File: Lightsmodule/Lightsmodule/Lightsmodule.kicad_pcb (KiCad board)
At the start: 2 copper layers, 69 x 45.5 mm, 33 parts, among them J1 Conn_01x02_Socket, J2 Conn_01x06_Socket, Q5 Q_NMOS_GSD, SW1 SW_Push_SPDT, SW2 SW_Push_SPDT, SW3 SW_Push_SPDT, SW6 SW_Push_SPDT, SW7 SW_Push_SPDT, SW8 SW_Push_SPDT, U1 TLC555xD, U2 TLP3553A, U3 TLP3553A

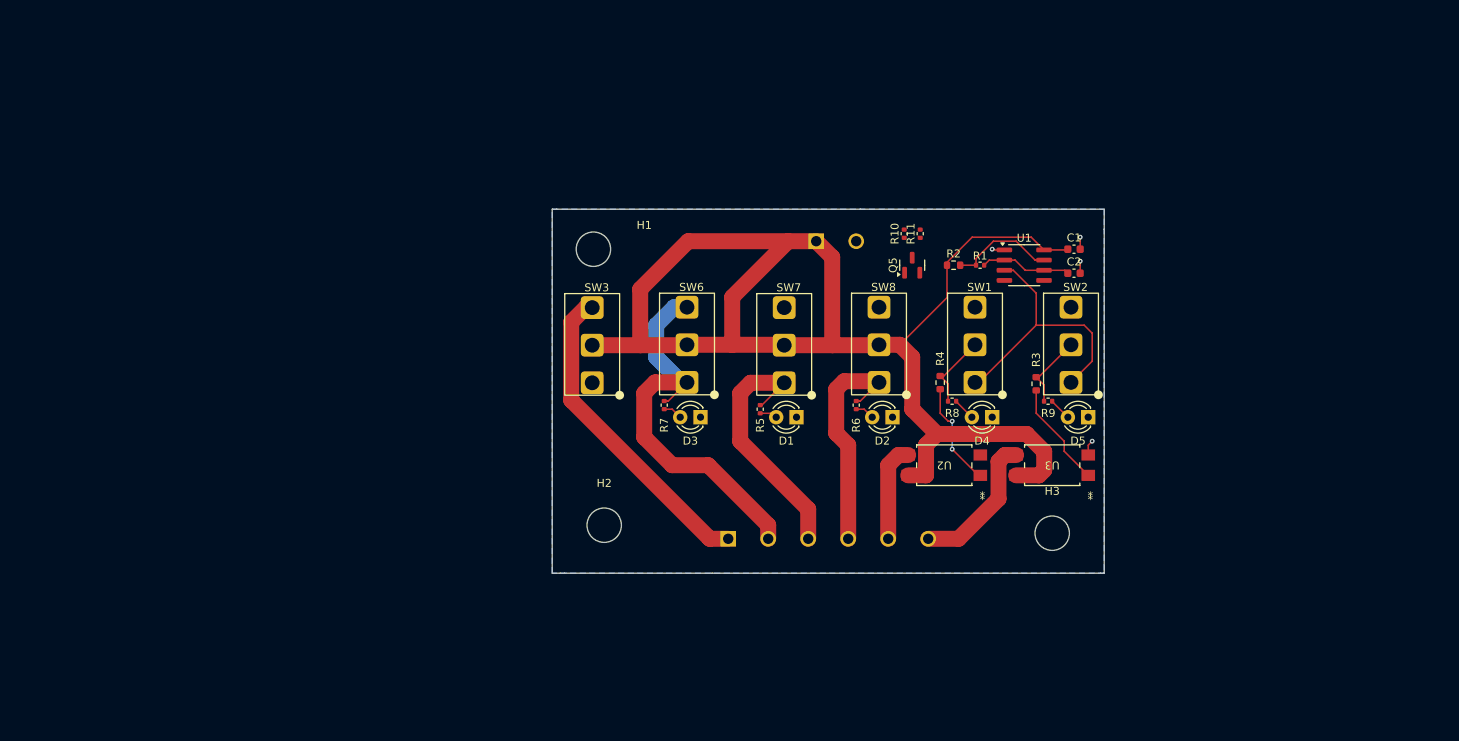
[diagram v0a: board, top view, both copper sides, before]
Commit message: In Theory working Timing / Buzzer Circuit
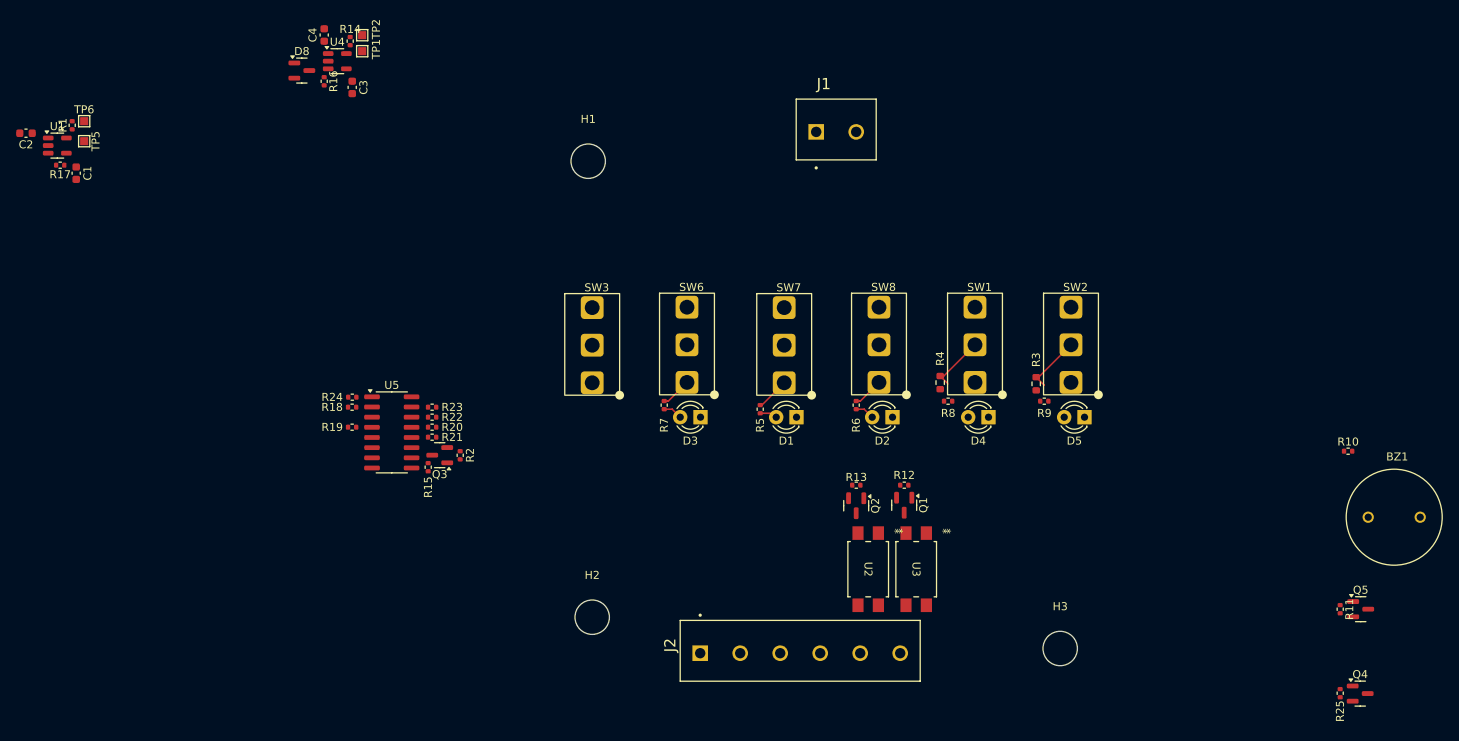
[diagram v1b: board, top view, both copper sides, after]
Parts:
- added BZ1: Buzzer, Library:CUI_CEM-1212S, F.Cu at (280.2, 116.5)
- added C3: 820n, Capacitor_SMD:C_0603_1608Metric, F.Cu at (150.0, 62.8)
- added C4: 820n, Capacitor_SMD:C_0603_1608Metric, F.Cu at (146.5, 56.2)
- added D8: D_Zener_Dual_CommonCathode_AAK, Package_TO_SOT_SMD:SOT-23, F.Cu at (143.7, 60.7)
- added Q1: Q_NMOS_GSD, Package_TO_SOT_SMD:SOT-23, F.Cu at (219.0, 115.0)
- added Q2: Q_NMOS_GSD, Package_TO_SOT_SMD:SOT-23, F.Cu at (213.0, 115.1)
- added Q3: Q_NMOS_GSD, Package_TO_SOT_SMD:SOT-23, F.Cu at (160.9, 108.8)
- added Q4: Q_NMOS_GSD, Package_TO_SOT_SMD:SOT-23, F.Cu at (276.0, 138.6)
- added R12: 325k, Resistor_SMD:R_0402_1005Metric, F.Cu at (219.0, 112.5)
- added R13: 325k, Resistor_SMD:R_0402_1005Metric, F.Cu at (213.0, 112.5)
- added R14: 325k, Resistor_SMD:R_0402_1005Metric, F.Cu at (149.8, 57.0)
- added R15: 325k, Resistor_SMD:R_0402_1005Metric, F.Cu at (159.5, 110.2)
- added R16: 820k, Resistor_SMD:R_0402_1005Metric, F.Cu at (146.5, 62.0)
- added R17: 820k, Resistor_SMD:R_0402_1005Metric, F.Cu at (113.5, 72.5)
- added R18: 0, Resistor_SMD:R_0402_1005Metric, F.Cu at (150.0, 102.8)
- added R19: 0, Resistor_SMD:R_0402_1005Metric, F.Cu at (150.0, 105.2)
- added R20: 0, Resistor_SMD:R_0402_1005Metric, F.Cu at (160.0, 105.2)
- added R21: 0, Resistor_SMD:R_0402_1005Metric, F.Cu at (160.0, 106.5)
- added R22: 0, Resistor_SMD:R_0402_1005Metric, F.Cu at (160.0, 104.0)
- added R23: 0, Resistor_SMD:R_0402_1005Metric, F.Cu at (160.0, 102.8)
- added R24: 0, Resistor_SMD:R_0402_1005Metric, F.Cu at (150.0, 101.5)
- added R25: 325k, Resistor_SMD:R_0402_1005Metric, F.Cu at (273.5, 138.5)
- added TP1: TestPoint, TestPoint:TestPoint_Pad_1.0x1.0mm, F.Cu at (151.2, 58.2)
- added TP2: TestPoint, TestPoint:TestPoint_Pad_1.0x1.0mm, F.Cu at (151.2, 56.2)
- added TP5: TestPoint, TestPoint:TestPoint_Pad_1.0x1.0mm, F.Cu at (116.5, 69.5)
- added TP6: TestPoint, TestPoint:TestPoint_Pad_1.0x1.0mm, F.Cu at (116.5, 67.0)
- added U4: MIC1553, Package_TO_SOT_SMD:SOT-23-5, F.Cu at (148.1, 59.5)
- added U5: MC14040BDR2G, Package_SO:SOIC-16_3.9x9.9mm_P1.27mm, F.Cu at (154.9, 105.9)
- C1, C2: value 470n -> 820n
- J1, J2: moved to F.Cu
- R1, R10: value 2M -> 820k
- R11: value 2M -> 325k
- R2: value 1.8k -> 325k; footprint Resistor_SMD:R_0603_1608Metric -> Resistor_SMD:R_0402_1005Metric
- U1: value TLC555xD -> MIC1553; footprint Package_SO:SOIC-8_3.9x4.9mm_P1.27mm -> Package_TO_SOT_SMD:SOT-23-5
- moved C2 132.2 mm to (109.2, 68.5), turned to 180 degrees
- moved C1 125.1 mm to (115.5, 73.5), turned to -90 degrees
- moved U1 121.8 mm to (113.1, 70.0)
- moved R1 114.8 mm to (115.0, 67.5), turned to 90 degrees
- moved Q5 70.7 mm to (276.1, 128.0), turned to 0 degrees
- moved R11 70.4 mm to (273.5, 128.0), turned to -90 degrees
- moved R2 66.1 mm to (163.5, 108.8), turned to 90 degrees
- moved R10 61.8 mm to (274.5, 108.2), turned to 0 degrees
- moved U3 21.4 mm to (220.5, 123.0), turned to -90 degrees
- moved U2 16.1 mm to (214.5, 123.0), turned to -90 degrees
- moved J2 14.7 mm to (193.5, 133.5)
- moved H3 14.4 mm to (238.5, 132.9)
- moved J1 13.7 mm to (208.0, 68.3)
- moved H2 11.6 mm to (180.0, 129.0)
- moved H1 11.0 mm to (179.5, 72.0)
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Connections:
- C2 pad 1: Net-(U1-THR) -> Net-(U1-T/T)
- Q5 pad 1: /OUT -> /BUZZ_DRV
- Q5 pad 2: GND -> Net-(Q4-D)
- R1 pad 1: Net-(U1-DIS) -> /1hz
- R1 pad 2: Net-(U1-THR) -> Net-(U1-T/T)
- R11 pad 1: /OUT -> /BUZZ_DRV
- R2 pad 1: +12V -> /1hz
- R2 pad 2: Net-(U1-DIS) -> GND
- R3 pad 1: /RIGHT_EN -> +12V
- R4 pad 1: /LEFT_EN -> +12V
- SW1 pad 1: /OUT -> /1hz
- SW2 pad 1: /OUT -> /1hz
- U1 pad 1: GND -> Net-(U1-T/T)
- U1 pad 2: Net-(U1-THR) -> GND
- U1 pad 3: /OUT -> Net-(U1-CS)
- U1 pad 5: unconnected-(U1-CV-Pad5) -> /1hz
- U2 pad 2: GND -> Net-(Q2-D)
- U3 pad 2: GND -> Net-(Q1-D)
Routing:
- net +12V: track 171.0 -> 0.22 mm
- net /BRIGHT: track 50.9 -> 3.81 mm
- net /HORN: track 39.9 -> 0.00 mm
- net /OUT: track 34.4 -> 0.00 mm
- net /HEADLIGHT: track 31.9 -> 4.16 mm
- net /FOG: track 29.0 -> 4.03 mm
- net /R_OUT: track 18.1 -> 0.00 mm
- net Net-(R3-Pad2): track 13.3 -> 0.00 mm
- net Net-(R4-Pad2): track 13.3 -> 0.00 mm, vias 2 -> 0
- net Net-(U1-DIS): track 13.2 -> 0.00 mm
- net /L_OUT: track 12.2 -> 0.00 mm
- net Net-(U1-THR): track 11.4 -> 0.00 mm
- net GND: track 6.50 -> 0.00 mm, vias 4 -> 0
- net Net-(D5-A): track 2.81 -> 0.00 mm
- net Net-(D4-A): track 2.81 -> 0.00 mm
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- removed copper zone on B.Cu, net GND
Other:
- board outline removed
- board text removed: "12V"
- board text removed: "BRIGHT"
- board text removed: "FOG"
- board text removed: "GND"
- board text removed: "HEADLIGHT"
- board text removed: "HORN"
- board text removed: "LEFT"
- board text removed: "RIGHT"

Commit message: First pass Layout
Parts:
- J1, J2: moved to B.Cu
- moved C2 136.2 mm to (237.7, 113.6), turned to 0 degrees
- moved R17 133.0 mm to (240.9, 110.4), turned to -90 degrees
- moved U1 131.8 mm to (238.5, 110.8), turned to 90 degrees
- moved C1 131.2 mm to (241.9, 108.4), turned to 0 degrees
- moved R1 127.8 mm to (236.0, 108.9), turned to 180 degrees
- moved TP5 127.2 mm to (237.9, 107.4), turned to 0 degrees
- moved TP6 125.6 mm to (235.4, 107.4), turned to 90 degrees
- moved C4 102.2 mm to (232.7, 111.0), turned to 0 degrees
- moved TP2 100.9 mm to (232.7, 115.8), turned to -90 degrees
- moved R14 100.2 mm to (232.0, 114.2), turned to 0 degrees
- moved TP1 98.1 mm to (230.7, 115.8), turned to -90 degrees
- moved U4 97.1 mm to (229.4, 112.6), turned to -90 degrees
- moved D8 97.0 mm to (228.3, 108.2), turned to -90 degrees
- moved R16 94.2 mm to (226.9, 111.0), turned to 180 degrees
- moved C3 92.1 mm to (226.2, 114.5), turned to 180 degrees
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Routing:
- net /BRIGHT: track 3.81 -> 62.0 mm
- net /FOG: track 4.03 -> 61.0 mm
- net /1hz: track 0.50 -> 55.3 mm, vias 0 -> 1
- net /HORN: track 0.00 -> 51.8 mm
- net /HEADLIGHT: track 4.16 -> 54.8 mm
- net /RIGHT_EN: track 8.77 -> 52.5 mm, vias 0 -> 2
- net /BUZZ_DRV: track 0.00 -> 40.3 mm, vias 0 -> 4
- net /LEFT_EN: track 7.35 -> 38.6 mm
- net /BUZZ_EN: track 0.00 -> 30.2 mm
- net GND: track 0.00 -> 23.7 mm, vias 0 -> 14
- net Net-(BZ1--): track 0.00 -> 15.9 mm
- net /L_OUT: track 0.00 -> 13.9 mm
- net +12V: track 0.22 -> 14.0 mm
- net Net-(U4-T/T): track 0.00 -> 10.4 mm
- net Net-(U1-T/T): track 0.00 -> 7.38 mm
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- added copper zone on F.Cu, net +12V
- added copper zone on B.Cu, net GND
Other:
- board outline added: 68.2 x 57.2 mm

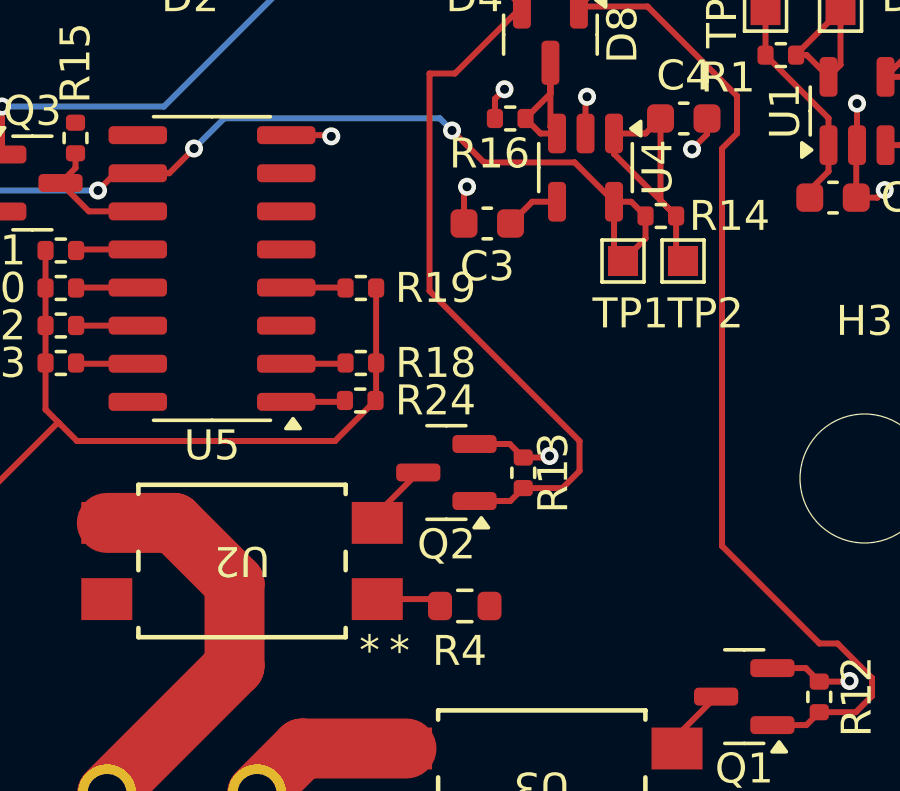
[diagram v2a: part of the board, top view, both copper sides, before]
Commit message: Silkscreen Change, Minor layout for better planes
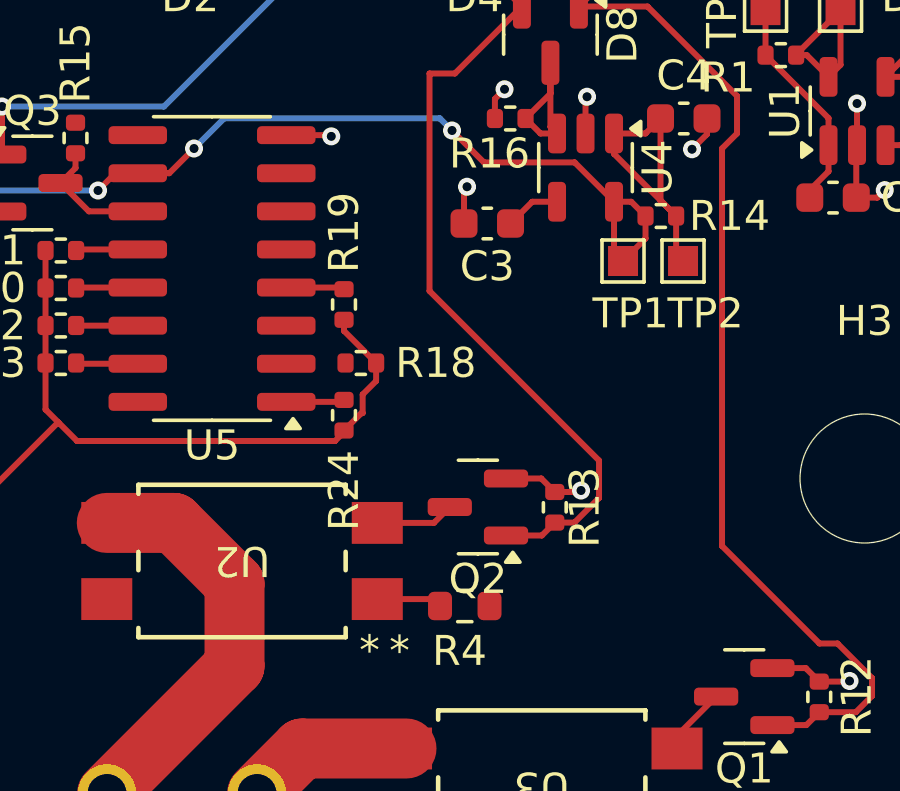
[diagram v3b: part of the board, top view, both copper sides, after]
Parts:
- moved Q2 1.56 mm to (225.9, 124.0)
- moved R13 1.56 mm to (228.4, 124.0)
- moved R19 0.78 mm to (221.4, 117.2), turned to -90 degrees
- moved R24 0.73 mm to (221.4, 120.9), turned to -90 degrees
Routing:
- net Net-(U5-Q6): track 1.99 -> 0.04 mm
- net /LEFT_EN: track 38.6 -> 39.4 mm
- net /BUZZ_EN: track 30.2 -> 29.6 mm
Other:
- board text added: "12V"
- board text added: "BRIGHT"
- board text added: "FOG/RUNNER"
- board text added: "GND"
- board text added: "HEADLIGHT"
- board text added: "HORN"
- board text added: "LEFT"
- board text added: "RIGHT"

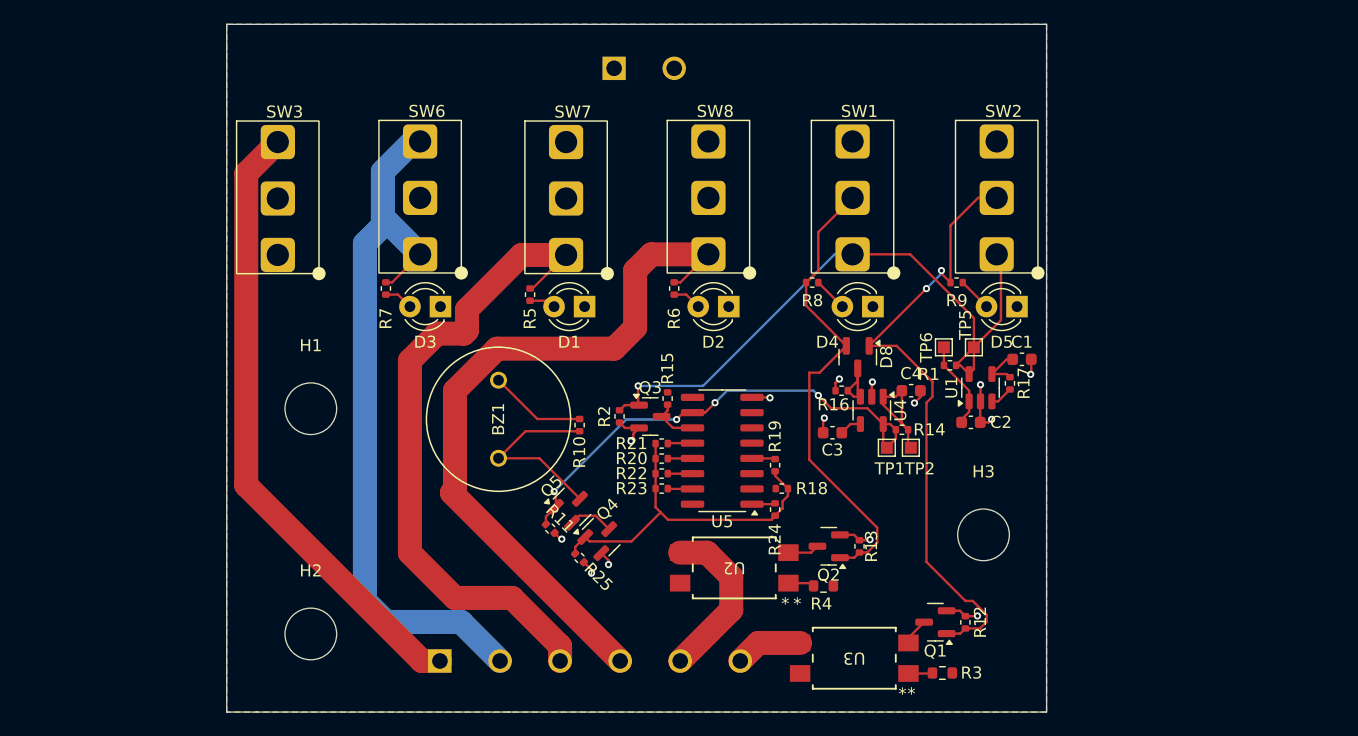
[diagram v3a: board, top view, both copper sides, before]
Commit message: New Layout based on more spread out Switches
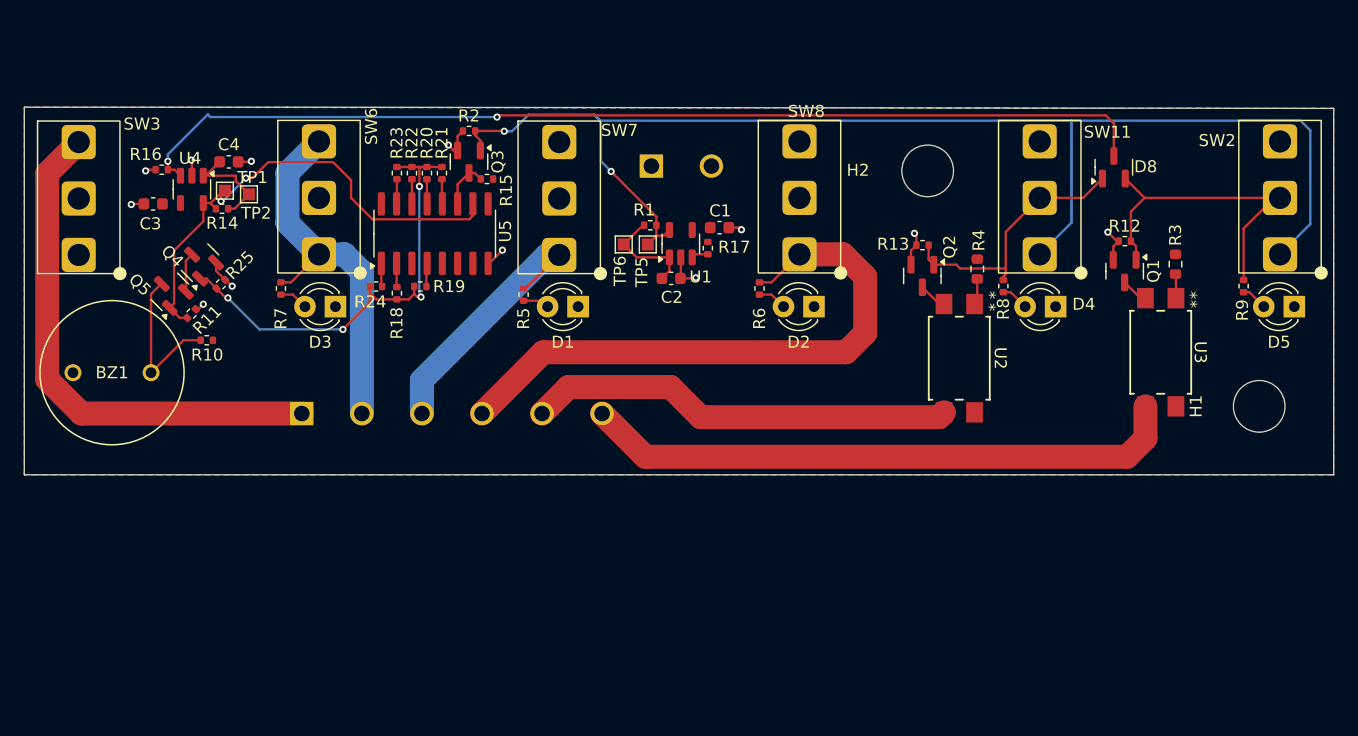
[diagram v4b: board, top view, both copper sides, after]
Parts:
- removed H3: MountingHole, MountingHole:MountingHole_4.3mm_M4
- moved H1 79.0 mm to (261.7, 112.3), turned to 90 degrees
- moved H2 64.2 mm to (234.1, 92.7)
- moved C4 59.9 mm to (175.9, 92.0)
- moved C3 59.7 mm to (169.6, 95.5)
- moved R14 59.5 mm to (175.4, 95.8)
- moved R16 59.5 mm to (170.3, 92.6)
- moved U4 59.5 mm to (172.8, 94.2)
- moved TP1 59.1 mm to (175.6, 94.3)
- moved TP2 59.0 mm to (177.6, 94.7)
- moved Q4 40.5 mm to (173.5, 100.3), turned to 135 degrees
- moved R3 39.2 mm to (254.7, 100.5), turned to -90 degrees
- moved R24 38.1 mm to (188.2, 102.3), turned to 180 degrees
- moved Q5 38.0 mm to (171.0, 102.8), turned to 135 degrees
- moved R25 37.6 mm to (175.3, 102.1), turned to 45 degrees
- moved U3 36.0 mm to (253.5, 107.8), turned to -90 degrees
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- renumbered SW1 to SW11
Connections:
- D8 pad 1: /RIGHT_EN -> /LEFT_EN
- D8 pad 2: /LEFT_EN -> /RIGHT_EN
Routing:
- net Net-(D8-K): track 5.91 -> 85.8 mm, vias 0 -> 2
- net /1hz: track 55.3 -> 110.6 mm, vias 1 -> 2
- net /R_OUT: track 5.60 -> 50.0 mm
- net /HEADLIGHT: track 54.8 -> 22.9 mm
- net /BRIGHT: track 62.0 -> 31.7 mm
- net /RIGHT_EN: track 52.5 -> 27.7 mm, vias 2 -> 0
- net /L_OUT: track 13.9 -> 35.6 mm
- net /LEFT_EN: track 39.4 -> 21.9 mm
- net +12V: track 14.0 -> 0.00 mm
- net /FOG: track 61.0 -> 49.9 mm
- net /BUZZ_EN: track 29.6 -> 38.7 mm, vias 0 -> 4
- net /HORN: track 51.8 -> 43.2 mm
- net Net-(BZ1--): track 15.9 -> 13.0 mm
- net Net-(U5-Q6): track 0.04 -> 1.99 mm
- net Net-(U4-T/T): track 10.4 -> 8.76 mm
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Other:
- board size 68.2 x 57.2 mm -> 109 x 30.6 mm

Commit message: DRC Checked PCB. Shipped
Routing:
- net /BUZZ_EN: track 38.7 -> 39.9 mm
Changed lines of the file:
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@@
 		(at 220 88.498982)
 		(property "Reference" "SW8"
-			(at 4 -0.75 0)
+			(at -1.85 1.226018 0)
 			(unlocked yes)
 			(layer "F.SilkS")
@@
 	)
 	(segment
-		(start 187.665 103.537)
-		(end 187.665 102.325)
+		(start 191.925 103.2)
+		(end 191.61 103.2)
 		(width 0.2)
 		(layer "F.Cu")
@@
 	)
 	(segment
-		(start 191.925 103.2)
-		(end 191.61 103.2)
+		(start 184.375 106.95)
+		(end 187.665 103.66)
 		(width 0.2)
 		(layer "F.Cu")
@@
 	)
 	(segment
-		(start 187.665 103.66)
-		(end 185.425 105.9)
+		(start 187.665 102.865)
+		(end 187.665 102.325)
 		(width 0.2)
 		(layer "F.Cu")
@@
 	)
 	(segment
-		(start 187.665 102.865)
-		(end 187.665 102.325)
+		(start 191.61 103.2)
+		(end 191.355 102.945)
 		(width 0.2)
 		(layer "F.Cu")
@@
 	)
 	(segment
-		(start 191.61 103.2)
-		(end 191.355 102.945)
+		(start 187.665 103.66)
+		(end 187.665 102.325)
 		(width 0.2)
 		(layer "F.Cu")
@@
 	)
 	(segment
-		(start 187.665 103.537)
-		(end 187.665 103.66)
-		(width 0.2)
-		(layer "F.Cu")
-		(net 30)
-	)
-	(segment
 		(start 193.665 92.375)
 		(end 192.415 92.375001)
@@
 	)
 	(via
-		(at 185.425 105.9)
+		(at 184.375 106.95)
 		(size 0.6)
 		(drill 0.3)
@@
 	)
 	(segment
+		(start 179.825 107.25)
+		(end 184.075 107.25)
+		(width 0.2)
+		(layer "B.Cu")
+		(net 30)
+	)
+	(segment
 		(start 191.789924 103.064924)
 		(end 191.925 103.2)
@@
 	)
 	(segment
-		(start 185.425 105.9)
-		(end 178.475 105.9)
+		(start 184.075 107.25)
+		(end 184.375 106.95)
+		(width 0.2)
+		(layer "B.Cu")
+		(net 30)
+	)
+	(segment
+		(start 178.475 105.9)
+		(end 179.825 107.25)
 		(width 0.2)
 		(layer "B.Cu")
